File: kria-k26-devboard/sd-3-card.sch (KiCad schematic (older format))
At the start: 20 parts, among them J6 1140084168, Q3 BSS123, Q4 AO3401A, U27 NVT4858HKZ, U28 TPS2116DRLR

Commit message: Progress in PCB placement
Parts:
- removed R64: 4x33R_0201_array, antmicro-footprints:EXB18V, symbol antmicroResistorNetworksArrays:4x33R_0201_array
- added R105, R117, R121, R17: R_33R_0402, antmicro-footprints:0402-res, symbol antmicroResistors0402:R_33R_0402
- renumbered C139 to C16, C140 to C17, C25 to C18, C141 to C19, C27 to C20, C146 to C21, C147 to C22, C143 to C23, C144 to C24, J6 to J2, Q3 to Q1, Q4 to Q2, R62 to R15, R63 to R16, R3 to R18, R66 to R19, R65 to R20, U27 to U4, U28 to U5
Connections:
- net MIO46: now also R17.1
- net MIO47: now also R105.1
- net MIO48: now also R117.1
- net MIO49: now also R121.1
- net at U4.1 (DAT2A): now also R117.2
- net at U4.2 (DAT3A): now also R121.2
- net at U4.3 (DAT0A): now also R17.2
- net at U4.4 (DAT1A): now also R105.2

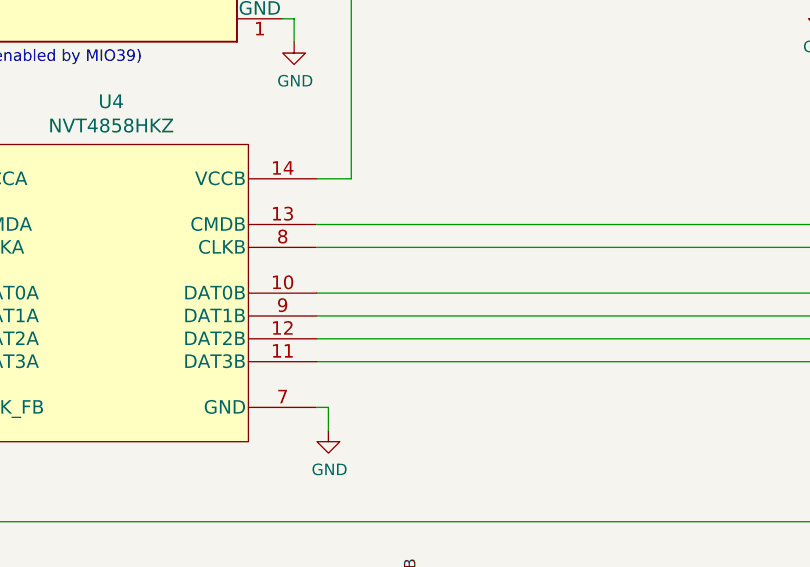
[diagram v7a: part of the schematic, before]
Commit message: Routed PS reset, improved SOM fanout, routed remaing SD 3.0 traces, component size optimization
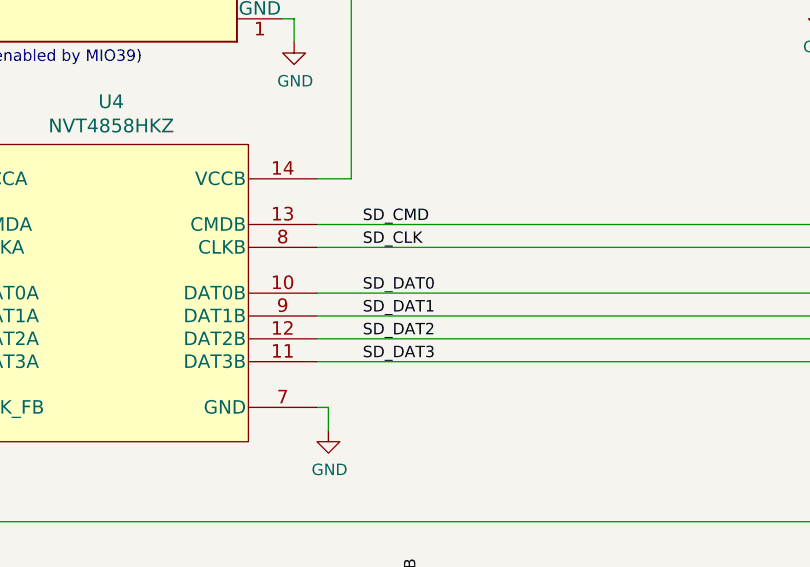
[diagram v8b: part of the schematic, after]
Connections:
- net SD_DAT0: now reaches J2.7 (DAT0), U4.10 (DAT0B)
- net SD_DAT3: now reaches J2.2 (CD/DAT3), U4.11 (DAT3B)
- net SD_DAT2: now reaches J2.1 (DAT2), U4.12 (DAT2B)
- net SD_CMD: now reaches J2.3 (CMD), U4.13 (CMDB)
- net SD_CLK: now reaches J2.5 (CLK), U4.8 (CLKB)
- net SD_DAT1: now reaches J2.8 (DAT1), U4.9 (DAT1B)
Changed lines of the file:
@@
 	1    0    0    -1
 $EndComp
+Text Label 5700 5300 0    50   ~ 0
+SD_DAT3
+Text Label 5700 5200 0    50   ~ 0
+SD_DAT2
+Text Label 5700 5100 0    50   ~ 0
+SD_DAT1
+Text Label 5700 5000 0    50   ~ 0
+SD_DAT0
 Wire Bus Line
 	2250 4450 2250 6000
+Text Label 5700 4700 0    50   ~ 0
+SD_CMD
+Text Label 5700 4800 0    50   ~ 0
+SD_CLK
 $EndSCHEMATC
